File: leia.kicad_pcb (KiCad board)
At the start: 4 copper layers, 43 x 66 mm, 90 parts, among them P1 GND, P1000 ISO7816_NO, P1900 CONN_FPC16, P3000 USB_FS_OTG, P513 TP1, P514 TP2, P515 TP3, P523 UART4, P542 TP4, P543 TP5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

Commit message: [cleanup] updating project files for LEIA
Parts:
- P1000: footprint wookey:VJW53666 -> leia:VJW53666
- P1900: footprint wookey:FPC16_MOLEX_52892_1633 -> leia:FPC16_MOLEX_52892_1633
- P3000, P6000: footprint wookey:USB_Micro-B-MOLEX_105017-0001 -> leia:USB_Micro-B-MOLEX_105017-0001
- SW503, SW514: footprint wookey:KSR_TACTILE_SWITCH -> leia:KSR_TACTILE_SWITCH
- U400: footprint wookey:SDCARD_DM3AT -> leia:SDCARD_DM3AT
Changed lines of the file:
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@@
     )
   )
-  (module wookey:USB_Micro-B-MOLEX_105017-0001 (layer F.Cu)
+  (module leia:USB_Micro-B-MOLEX_105017-0001 (layer F.Cu)
     (at 127.50844 76.4031 90)
     (descr "Micro USB Type B Receptacle")
@@
     )
   )
-  (module wookey:USB_Micro-B-MOLEX_105017-0001 (layer F.Cu)
+  (module leia:USB_Micro-B-MOLEX_105017-0001 (layer F.Cu)
     (at 127.50844 45.9222 90)
     (descr "Micro USB Type B Receptacle")
@@
       (solder_mask_margin 0.77) (clearance 0.77))
   )
-  (module wookey:VJW53666 locked (layer B.Cu)
+  (module leia:VJW53666 locked (layer B.Cu)
     (at 110.28844 49.8831 90)
     (fp_text reference P1000 (at -5.8191 8.39306 90) (layer B.SilkS)
@@
     )
   )
-  (module wookey:FPC16_MOLEX_52892_1633 (layer F.Cu)
+  (module leia:FPC16_MOLEX_52892_1633 (layer F.Cu)
     (at 94.0943 97.0407)
     (descr http://www.farnell.com/datasheets/2138527.pdf)
@@
     )
   )
-  (module wookey:KSR_TACTILE_SWITCH (layer B.Cu)
+  (module leia:KSR_TACTILE_SWITCH (layer B.Cu)
     (at 113.247748 41.86941 90)
     (fp_text reference SW503 (at -2.49423 3.917372) (layer B.SilkS)
@@
     )
   )
-  (module wookey:KSR_TACTILE_SWITCH (layer B.Cu)
+  (module leia:KSR_TACTILE_SWITCH (layer B.Cu)
     (at 104.39844 41.8731 270)
     (fp_text reference SW514 (at 2.49816 3.49186 180) (layer B.SilkS)
@@
     )
   )
-  (module wookey:SDCARD_DM3AT (layer F.Cu)
+  (module leia:SDCARD_DM3AT (layer F.Cu)
     (at 120.21058 95.11538 90)
     (fp_text reference U400 (at -6.372056 -9.00914 270) (layer F.SilkS)

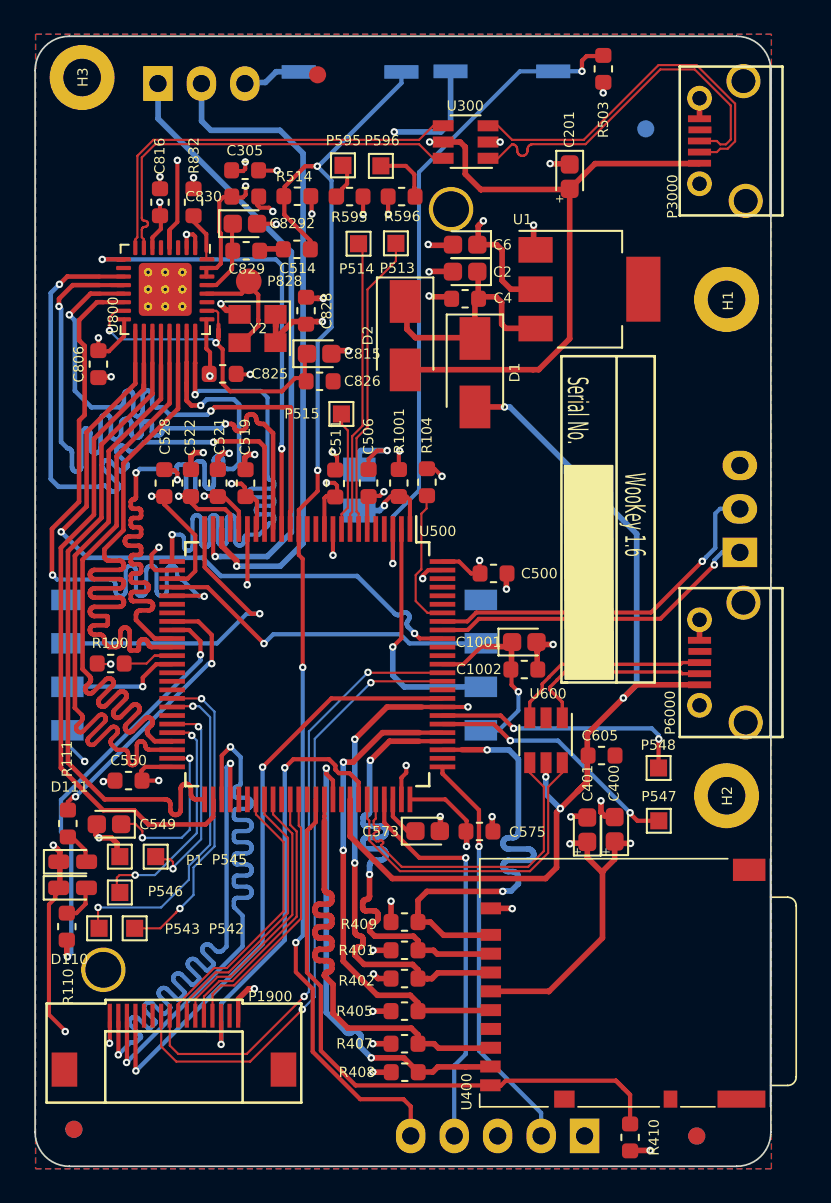
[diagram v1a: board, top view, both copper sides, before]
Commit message: [enhancement] Adding rshunt
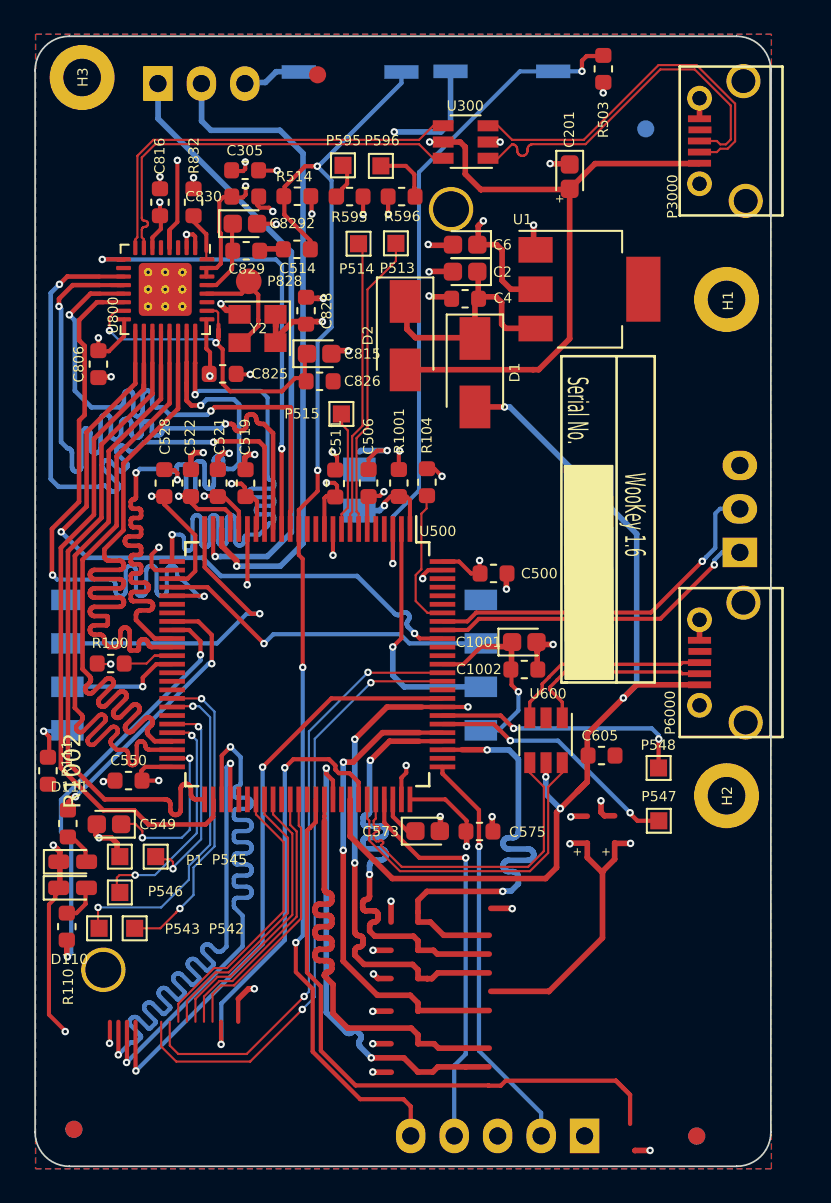
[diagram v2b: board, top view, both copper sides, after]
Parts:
- removed C400: 10uF 10V, Capacitor_Tantalum_SMD:CP_EIA-1608-08_AVX-J
- removed C401: 0.1uF 6,3V, Capacitor_Tantalum_SMD:CP_EIA-1608-08_AVX-J
- removed P1900: CONN_FPC16, leia:FPC16_MOLEX_52892_1633
- removed R401, R402, R405, R407, R408, R409, R410: 47K, Resistor_SMD:R_0603_1608Metric
- removed U400: MICROSDCARD, leia:SDCARD_DM3AT
- added R1002: 10, Resistor_SMD:R_0603_1608Metric, F.Cu at (86.7, 82.7)
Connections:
- P1000 pad C5: GND -> Net-(P1000-PadC5)
- U500 pad 53: /cpu/SPI_MISO -> (no net)
- U500 pad 54: /cpu/SPI_MOSI -> (no net)
- U500 pad 57: /cpu/~SPI_TOUCH_CS -> (no net)
- U500 pad 58: /cpu/TOUCH_BUSY -> (no net)
- U500 pad 59: /cpu/TOUCH_IRQ -> (no net)
- U500 pad 61: /cpu/SCREEN_~D~C -> (no net)
- U500 pad 62: /screen/SCREEN_RESET -> (no net)
- U500 pad 64: /cpu/SD_D7 -> (no net)
- U500 pad 65: /cpu/SD_D0 -> (no net)
- U500 pad 66: /cpu/SD_D1 -> (no net)
- U500 pad 69: /cpu/~SPI_SCREEN_CS -> (no net)
- U500 pad 78: /cpu/SD_D2 -> (no net)
- U500 pad 79: /cpu/SD_D3 -> (no net)
- U500 pad 80: /cpu/SD_CLK -> (no net)
- U500 pad 83: /cpu/SD_CMD -> (no net)
- U500 pad 84: /cpu/SPI_SCK -> (no net)
- U500 pad 86: /cpu/~SPI_FLASH_CS -> (no net)
- U500 pad 87: /cpu/~SPI_FONT_CS -> (no net)
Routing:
- net (no net): track 0.00 -> 493.1 mm, vias 0 -> 23
- net /cpu/SD_D7: track 37.5 -> 0.00 mm
- net /cpu/~SPI_FLASH_CS: track 36.3 -> 0.00 mm, vias 2 -> 0
- net /cpu/SPI_MOSI: track 35.9 -> 0.00 mm, vias 2 -> 0
- net /cpu/SPI_SCK: track 35.9 -> 0.00 mm, vias 2 -> 0
- net /cpu/SPI_MISO: track 35.8 -> 0.00 mm, vias 2 -> 0
- net /cpu/~SPI_FONT_CS: track 35.7 -> 0.00 mm, vias 2 -> 0
- net /cpu/SD_CMD: track 29.4 -> 0.00 mm, vias 3 -> 0
- net /cpu/SD_D2: track 28.2 -> 0.00 mm, vias 2 -> 0
- net /cpu/SD_CLK: track 28.2 -> 0.00 mm, vias 2 -> 0
- net /cpu/SD_D0: track 28.1 -> 0.00 mm
- net /cpu/SD_D3: track 28.0 -> 0.00 mm, vias 2 -> 0
- net /cpu/SD_D1: track 27.9 -> 0.00 mm, vias 2 -> 0
- net /cpu/~SPI_SCREEN_CS: track 25.3 -> 0.00 mm, vias 2 -> 0
- net /cpu/~SPI_TOUCH_CS: track 16.7 -> 0.00 mm
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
